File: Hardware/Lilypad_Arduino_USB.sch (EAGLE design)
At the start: 45 parts, among them U1 MCP73831, U2 MIC5219, U3 ATMEGA32U41:1, Y1 8MHz

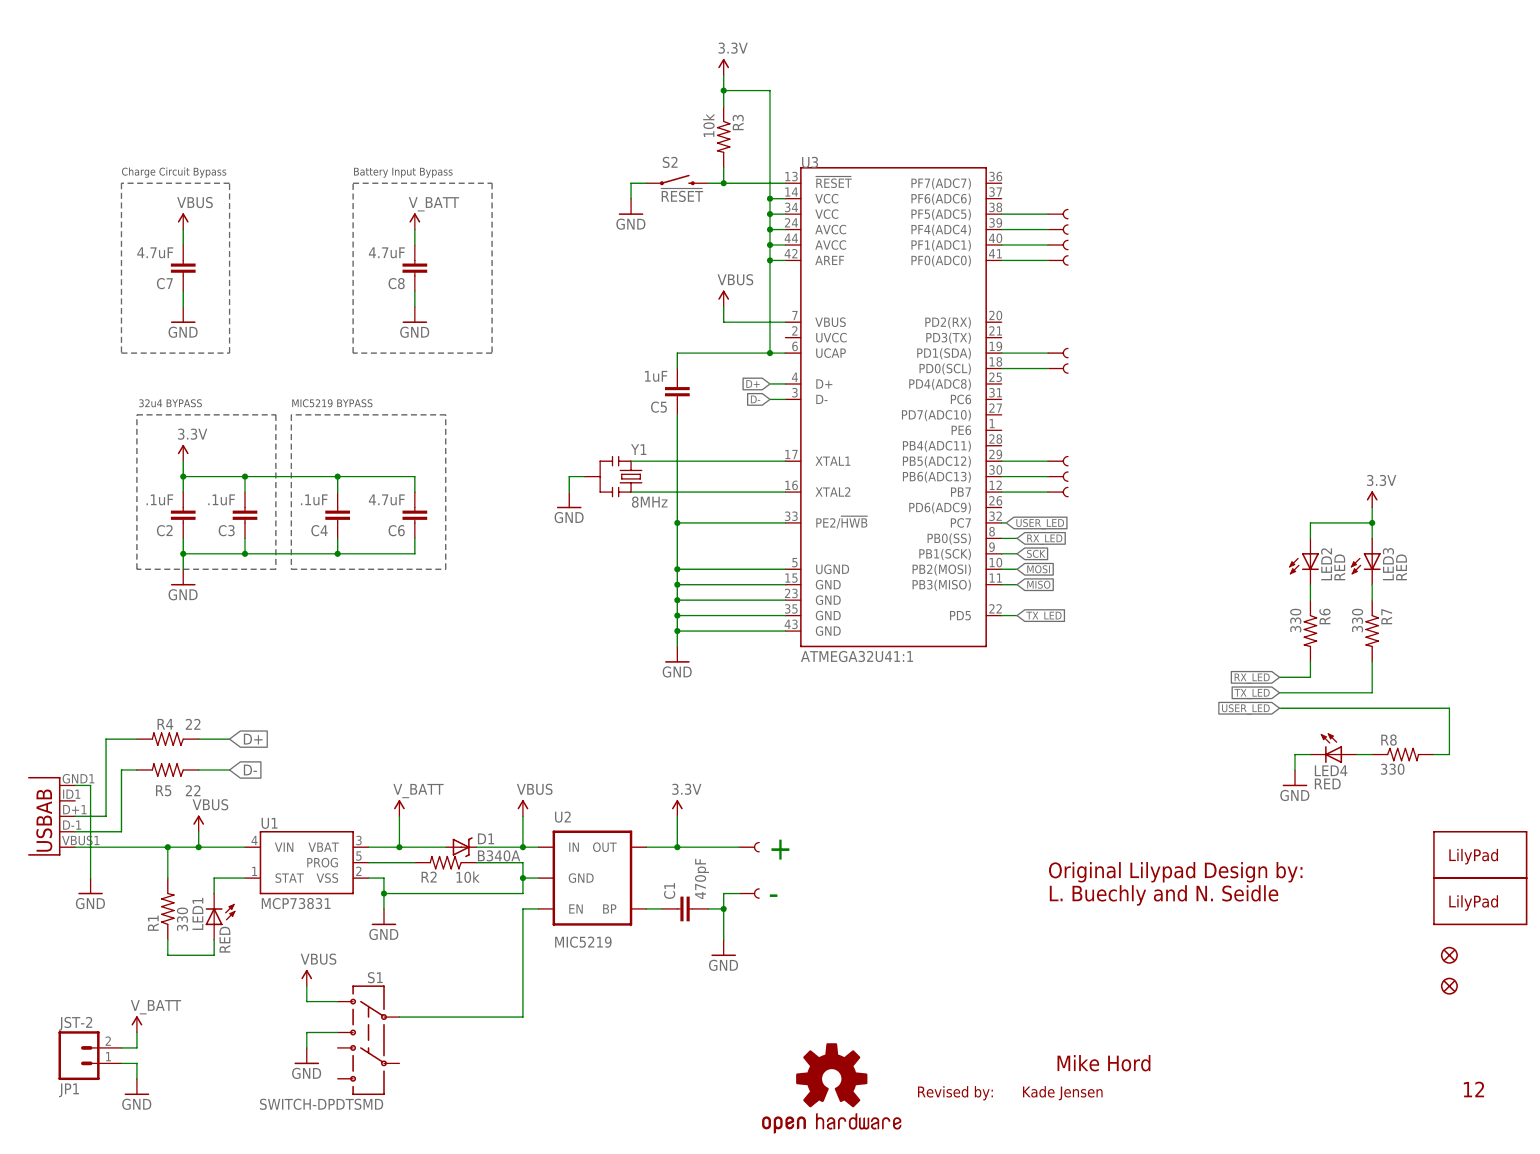
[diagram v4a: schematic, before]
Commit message: More updated packages
1.) New 0603 LED packages
2.) New resonator package
3.) Moved reset button over to allow silk to be correct size.
4.) Added attribution to board file
5.) Minor trace reroutes for new packages
6.) New 32u4 package variant that changes paste layer.
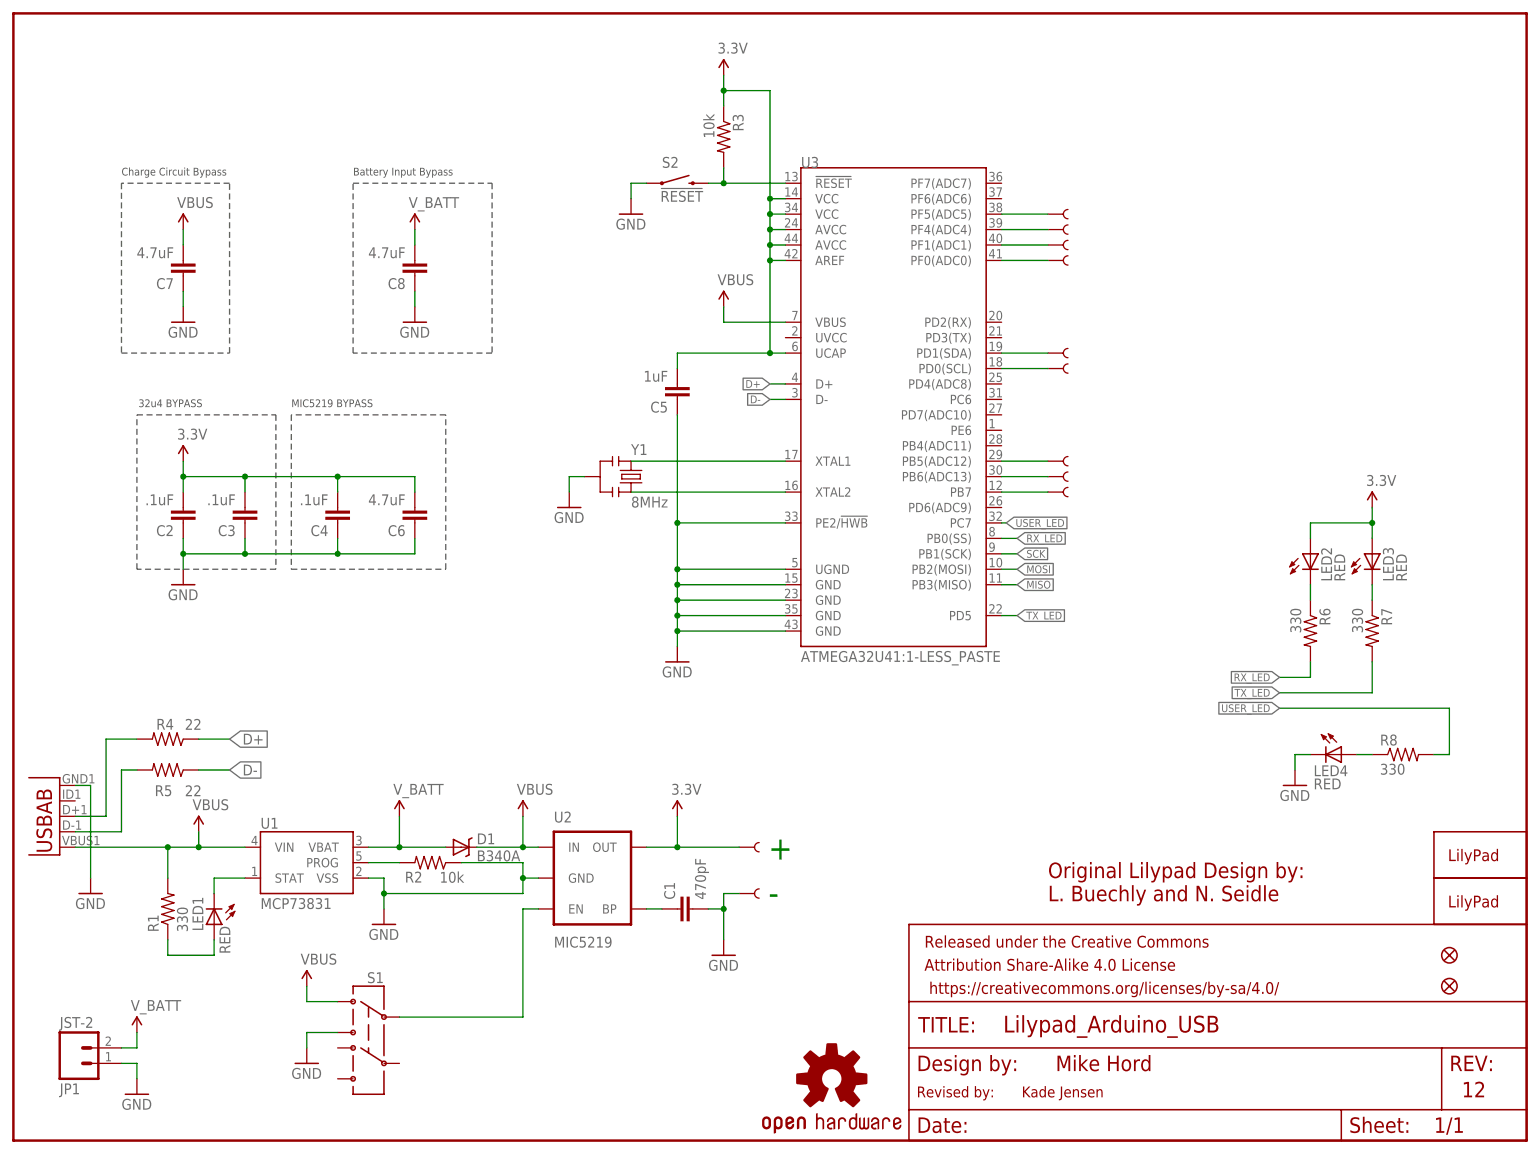
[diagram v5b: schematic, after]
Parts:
- removed X1: (no value), Testing:USB-AB"""
- added FRAME1: FRAME-LETTER, SparkFun-Aesthetics:FRAME-LETTER
- added U5: (no value), SparkFun-Connectors:USB-ABCONN-11794
- D1: device SparkFun-DiscreteSemi:DIODE-SCHOTTKY_ -> SparkFun-DiscreteSemi:DIODE-SCHOTTKY-B340A; PROD_ID DIO-09886 -> (none)
- S1: value SWITCH-DPDTSMD -> (none); device SparkFun-Electromechanical:SWITCH-DPDTSMD -> SparkFun-Electromechanical:SWITCH-DPDTAYZ0202
- U2: device SparkFun-PowerIC:V_REG_MIC5219SMD -> SparkFun-PowerIC:V_REG_MIC52193.3V
- U3: value ATMEGA32U41:1 -> ATMEGA32U41:1-LESS_PASTE; device Testing:ATMEGA32U41:1 -> Testing:ATMEGA32U41:1-LESS_PASTE
- Y1: device SparkFun-FreqCtrl:RESONATORSMD -> SparkFun-FreqCtrl:RESONATOR8MHZ
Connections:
- net 5V: now also U5.VBUS; no longer X1.VBUS
- net GND: now also U5.GND; no longer X1.GND
- net N$19: now also U5.D-; no longer X1.D-
- net N$20: now also U5.D+; no longer X1.D+
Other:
- moved on the sheet: R2
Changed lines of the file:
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@@
 <?xml version="1.0" encoding="utf-8"?>
 <!DOCTYPE eagle SYSTEM "eagle.dtd">
-<eagle version="6.4">
+<eagle version="6.5.0">
 <drawing>
 <settings>
@@
 <attribute name="NO_PART" value="1"/>
 </part>
-<part name="U3" library="Testing" deviceset="ATMEGA32U4" device="1:1">
+<part name="U3" library="Testing" deviceset="ATMEGA32U4" device="1:1-LESS_PASTE" value="ATMEGA32U41:1-LESS_PASTE">
 <attribute name="PROD_ID" value="IC-10828"/>
 </part>
@@
 <attribute name="PROD_ID" value="IC-09995"/>
 </part>
-<part name="U2" library="SparkFun-PowerIC" deviceset="V_REG_MIC5219" device="SMD" value="MIC5219">
+<part name="U2" library="SparkFun-PowerIC" deviceset="V_REG_MIC5219" device="3.3V" value="MIC5219">
 <attribute name="PROD_ID" value="VREG-09872"/>
 </part>
@@
 <attribute name="PROD_ID" value="CONN-08352"/>
 </part>
-<part name="X1" library="Testing" deviceset="USB-AB" device="&quot;&quot;&quot;"/>
 <part name="LED1" library="SparkFun-LED" deviceset="LED" device="0603" value="RED">
 <attribute name="PROD_ID" value="DIO-00819"/>
@@
 <attribute name="PROD_ID" value="RES-00818"/>
 </part>
-<part name="S1" library="SparkFun-Electromechanical" deviceset="SWITCH-DPDT" device="SMD">
+<part name="S1" library="SparkFun-Electromechanical" deviceset="SWITCH-DPDT" device="AYZ0202">
 <attribute name="PROD_ID" value="SWCH-08179"/>
 </part>
@@
 <attribute name="PROD_ID" value="CAP-10300"/>
 </part>
-<part name="Y1" library="SparkFun-FreqCtrl" deviceset="RESONATOR" device="SMD" value="8MHz">
+<part name="Y1" library="SparkFun-FreqCtrl" deviceset="RESONATOR" device="8MHZ" value="8MHz">
 <attribute name="PROD_ID" value="XTAL-08895"/>
 </part>
@@
 <part name="JP2" library="SparkFun" deviceset="FIDUCIAL" device="1X2"/>
 <part name="JP3" library="SparkFun" deviceset="FIDUCIAL" device="1X2"/>
-<part name="D1" library="SparkFun-DiscreteSemi" deviceset="DIODE-SCHOTTKY" device="_" value="B340A">
-<attribute name="PROD_ID" value="DIO-09886"/>
-</part>
 <part name="U$2" library="SparkFun-Aesthetics" deviceset="5V" device="" value="VBUS"/>
 <part name="U$3" library="SparkFun-Aesthetics" deviceset="5V" device="" value="VBUS"/>
@@
 <part name="GND12" library="SparkFun-Aesthetics" deviceset="GND" device=""/>
 <part name="U$5" library="SparkFun" deviceset="OSHW-LOGO" device="M"/>
+<part name="D1" library="SparkFun-DiscreteSemi" deviceset="DIODE-SCHOTTKY" device="-B340A" value="B340A"/>
+<part name="U5" library="SparkFun-Connectors" deviceset="USB-AB" device="CONN-11794"/>
 </parts>
 <sheets>
@@
 <attribute name="PROD_ID" x="10.16" y="15.24" size="1.27" layer="96" rot="MR180" display="off"/>
 </instance>
-<instance part="X1" gate="G$1" x="5.08" y="53.34" rot="MR0"/>
 <instance part="LED1" gate="G$1" x="33.02" y="35.56" smashed="yes" rot="R180">
 <attribute name="PROD_ID" x="33.02" y="35.56" size="1.27" layer="96" rot="R180" display="off"/>
@@
 <instance part="P+1" gate="G$1" x="109.22" y="53.34"/>
 <instance part="U$14" gate="G$1" x="63.5" y="53.34"/>
-<instance part="R2" gate="G$1" x="71.12" y="45.72" smashed="yes" rot="R180">
-<attribute name="PROD_ID" x="71.12" y="45.72" size="1.27" layer="96" rot="R180" display="off"/>
-<attribute name="NAME" x="69.85" y="44.2214" size="1.778" layer="95" rot="R180"/>
-<attribute name="VALUE" x="76.708" y="44.196" size="1.778" layer="96" rot="R180"/>
+<instance part="R2" gate="G$1" x="68.58" y="45.72" smashed="yes" rot="R180">
+<attribute name="PROD_ID" x="68.58" y="45.72" size="1.27" layer="96" rot="R180" display="off"/>
+<attribute name="NAME" x="67.31" y="44.2214" size="1.778" layer="95" rot="R180"/>
+<attribute name="VALUE" x="74.168" y="44.196" size="1.778" layer="96" rot="R180"/>
 </instance>
 <instance part="GND4" gate="1" x="116.84" y="30.48"/>
@@
 <instance part="JP2" gate="G$1" x="236.22" y="30.48"/>
 <instance part="JP3" gate="G$1" x="236.22" y="25.4"/>
-<instance part="D1" gate="G$1" x="73.66" y="48.26">
-<attribute name="PROD_ID" x="73.66" y="48.26" size="1.778" layer="96" display="off"/>
-</instance>
 <instance part="U$2" gate="G$1" x="83.82" y="53.34"/>
 <instance part="U$3" gate="G$1" x="48.26" y="25.4"/>
@@
 <instance part="GND12" gate="1" x="210.82" y="58.42"/>
 <instance part="U$5" gate="G$1" x="134.62" y="10.16"/>
+<instance part="D1" gate="G$1" x="73.66" y="48.26" smashed="yes">
+<attribute name="NAME" x="76.2" y="48.7426" size="1.778" layer="95"/>
+<attribute name="VALUE" x="76.2" y="45.9486" size="1.778" layer="96"/>
+</instance>
+<instance part="U5" gate="G$1" x="5.08" y="53.34" rot="MR0"/>
 </instances>
 <busses>
@@
 <segment>
 <pinref part="U1" gate="G$1" pin="VBAT"/>
-<pinref part="U$14" gate="G$1" pin="1.8V"/>
+<pinref part="U$14" gate="G$1" pin="V_BATT"/>
 <wire x1="58.42" y1="48.26" x2="63.5" y2="48.26" width="0.1524" layer="91"/>
 <wire x1="63.5" y1="53.34" x2="63.5" y2="48.26" width="0.1524" layer="91"/>
@@
 </segment>
 <segment>
-<pinref part="U$18" gate="G$1" pin="1.8V"/>
+<pinref part="U$18" gate="G$1" pin="V_BATT"/>
 <wire x1="66.04" y1="149.86" x2="66.04" y2="147.32" width="0.1524" layer="91"/>
 <pinref part="C8" gate="G$1" pin="2"/>
@@
 <wire x1="17.78" y1="15.24" x2="20.32" y2="15.24" width="0.1524" layer="91"/>
 <wire x1="20.32" y1="15.24" x2="20.32" y2="17.78" width="0.1524" layer="91"/>
-<pinref part="U$4" gate="G$1" pin="1.8V"/>
+<pinref part="U$4" gate="G$1" pin="V_BATT"/>
 </segment>
 </net>
@@
 <wire x1="83.82" y1="43.18" x2="86.36" y2="43.18" width="0.1524" layer="91"/>
 <pinref part="R2" gate="G$1" pin="1"/>
-<wire x1="76.2" y1="45.72" x2="83.82" y2="45.72" width="0.1524" layer="91"/>
+<wire x1="73.66" y1="45.72" x2="83.82" y2="45.72" width="0.1524" layer="91"/>
 <wire x1="83.82" y1="45.72" x2="83.82" y2="43.18" width="0.1524" layer="91"/>
 <junction x="83.82" y="43.18"/>
@@
 <pinref part="GND3" gate="1" pin="GND"/>
 <wire x1="12.7" y1="43.18" x2="12.7" y2="58.42" width="0.1524" layer="91"/>
-<pinref part="X1" gate="G$1" pin="GND"/>
 <wire x1="12.7" y1="58.42" x2="10.16" y2="58.42" width="0.1524" layer="91"/>
+<pinref part="U5" gate="G$1" pin="GND"/>
 </segment>
 </net>
@@
 <pinref part="R2" gate="G$1" pin="2"/>
 <pinref part="U1" gate="G$1" pin="PROG"/>
-<wire x1="66.04" y1="45.72" x2="58.42" y2="45.72" width="0.1524" layer="91"/>
+<wire x1="63.5" y1="45.72" x2="58.42" y2="45.72" width="0.1524" layer="91"/>
 </segment>
 </net>
@@
 </segment>
 <segment>
-<pinref part="X1" gate="G$1" pin="VBUS"/>
 <pinref part="U1" gate="G$1" pin="VIN"/>
 <wire x1="10.16" y1="48.26" x2="25.4" y2="48.26" width="0.1524" layer="91"/>
@@
 <junction x="30.48" y="48.26"/>
 <wire x1="30.48" y1="50.8" x2="30.48" y2="48.26" width="0.1524" layer="91"/>
+<pinref part="U5" gate="G$1" pin="VBUS"/>
 </segment>
 <segment>
@@
 </segment>
 <segment>
-<pinref part="D1" gate="G$1" pin="C"/>
 <pinref part="U2" gate="G$1" pin="IN"/>
-<wire x1="76.2" y1="48.26" x2="83.82" y2="48.26" width="0.1524" layer="91"/>
 <pinref part="U$2" gate="G$1" pin="5V"/>
 <wire x1="83.82" y1="48.26" x2="86.36" y2="48.26" width="0.1524" layer="91"/>
 <wire x1="83.82" y1="53.34" x2="83.82" y2="48.26" width="0.1524" layer="91"/>
+<pinref part="D1" gate="G$1" pin="C"/>
+<wire x1="83.82" y1="48.26" x2="76.2" y2="48.26" width="0.1524" layer="91"/>
 <junction x="83.82" y="48.26"/>
 </segment>
@@
 <wire x1="20.32" y1="60.96" x2="17.78" y2="60.96" width="0.1524" layer="91"/>
 <wire x1="17.78" y1="60.96" x2="17.78" y2="50.8" width="0.1524" layer="91"/>
-<pinref part="X1" gate="G$1" pin="D-"/>
 <wire x1="17.78" y1="50.8" x2="10.16" y2="50.8" width="0.1524" layer="91"/>
+<pinref part="U5" gate="G$1" pin="D-"/>
 </segment>
 </net>
@@
 <wire x1="20.32" y1="66.04" x2="15.24" y2="66.04" width="0.1524" layer="91"/>
 <wire x1="15.24" y1="53.34" x2="15.24" y2="66.04" width="0.1524" layer="91"/>
-<pinref part="X1" gate="G$1" pin="D+"/>
 <wire x1="10.16" y1="53.34" x2="15.24" y2="53.34" width="0.1524" layer="91"/>
-</segment>
-</net>
+<pinref part="U5" gate="G$1" pin="D+"/>
+</segment>
+</net>
